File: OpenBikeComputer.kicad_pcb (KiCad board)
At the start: 4 copper layers, 80 x 80 mm, 53 parts, among them J1 USB_C_Receptacle_USB2.0_14P, J2 RJ45_Shielded, J4 Micro_SD_Card_Det1, J5 Conn_01x24_Socket, J6 Conn_01x03_Pin, J7 RFShield_TwoPieces, J8 Conn_01x02_Socket, U1 nRF54L15-QFXX, U2 nPM1300-QEXX, U3 BQ298012RUGR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

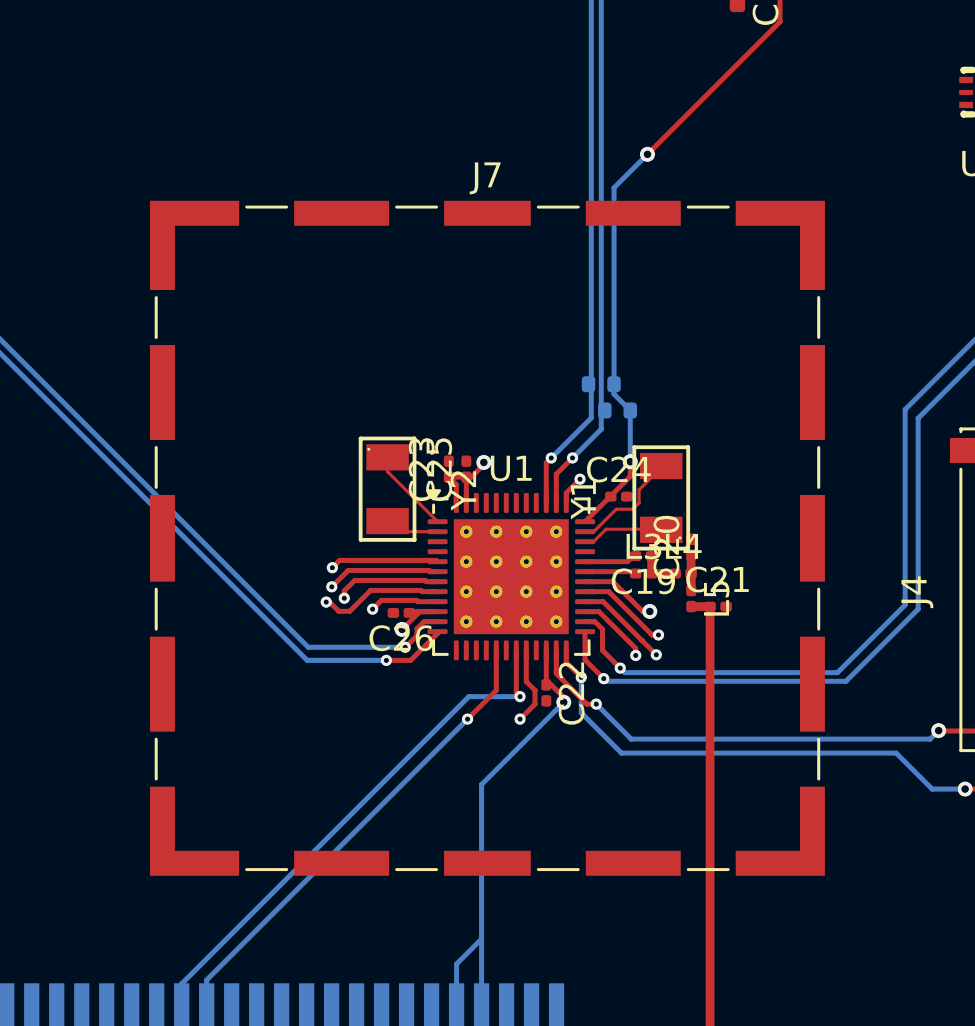
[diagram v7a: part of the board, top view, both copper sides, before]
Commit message: change RF shield
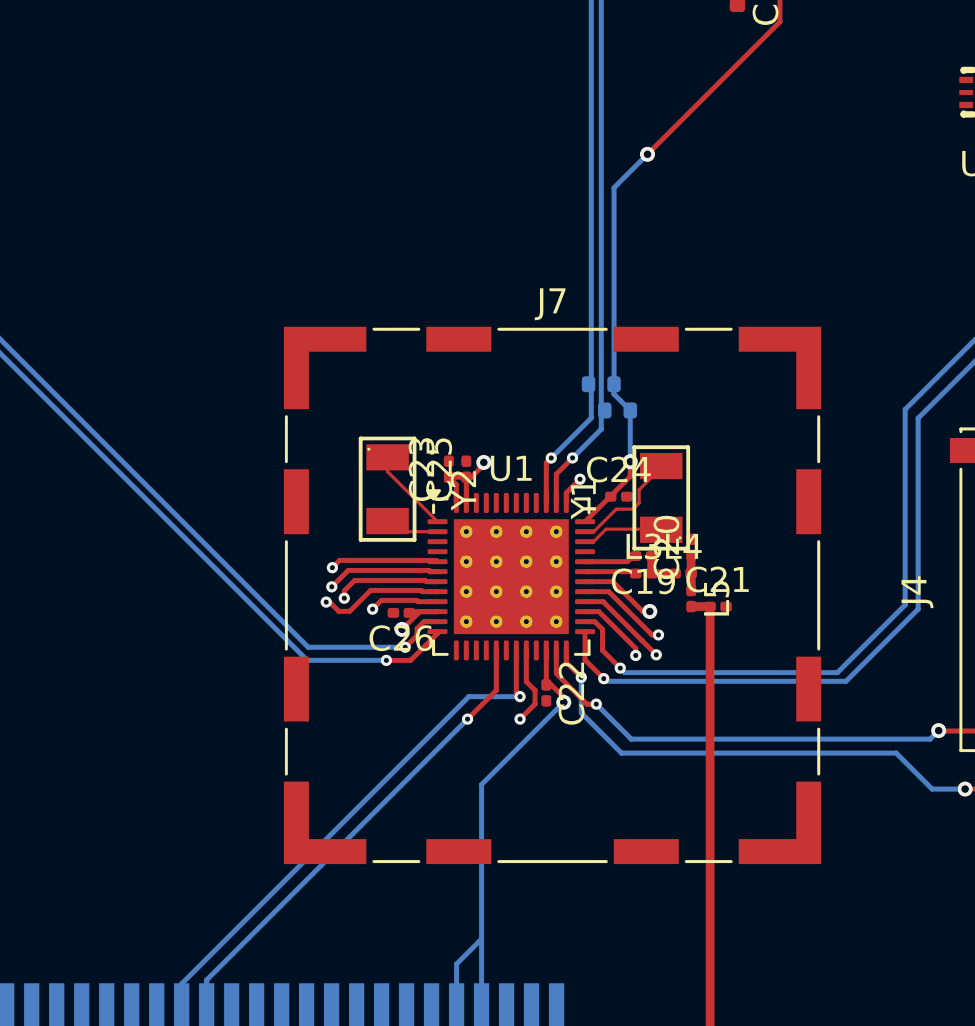
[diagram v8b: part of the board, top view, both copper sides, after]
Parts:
- J7: footprint RF_Shielding:Laird_Technologies_BMI-S-103_26.21x26.21mm -> RF_Shielding:Wuerth_36103205_20x20mm
- moved J7 3.47 mm to (201.6, 114.9)
